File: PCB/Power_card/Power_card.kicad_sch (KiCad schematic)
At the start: 55 parts, among them J1 Conn_01x01_Pin, J2 Conn_01x01_Pin, J3 Conn_01x01_Pin, J4 Conn_01x01_Pin, J5 Conn_01x01_Pin, J6 Conn_01x01_Pin, J7 Conn_02x04_Counter_Clockwise, J8 Conn_01x01_Pin, K1 Relay_SPST-NO, K2 Relay_SPST-NO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

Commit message: Ajout crystal
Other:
- note added: "Power card for touch switch"
- note removed: "Touch switch prototype"

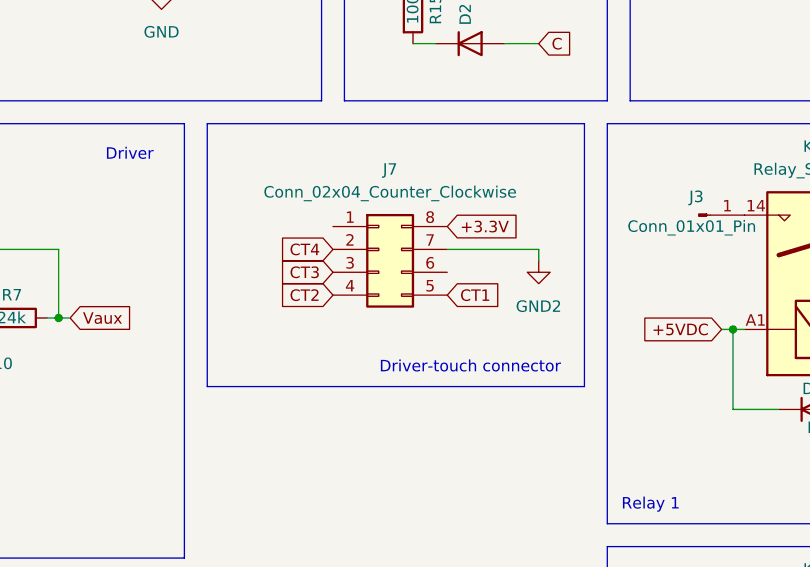
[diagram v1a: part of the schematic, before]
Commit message: Changement de connecteurs
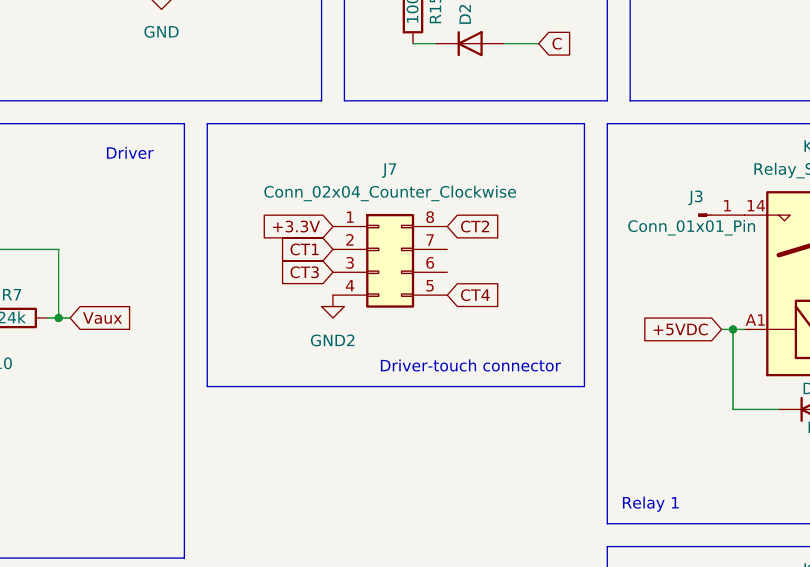
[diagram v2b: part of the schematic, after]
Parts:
- J7: footprint Connector_PinSocket_2.54mm:PinSocket_2x04_P2.54mm_Vertical -> Touch_Switch_Custom:Pin femelle
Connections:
- net +3.3V: now also J7.1 (Pin_1); no longer J7.8 (Pin_8)
- net CT1: now also J7.2 (Pin_2); no longer J7.5 (Pin_5)
- net CT2: now also J7.8 (Pin_8); no longer J7.4 (Pin_4)
- net CT4: now also J7.5 (Pin_5); no longer J7.2 (Pin_2)
- net GND2: now also J7.4 (Pin_4); no longer J7.7 (Pin_7)
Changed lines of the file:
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@@
 	(wire
 		(pts
-			(xy 137.16 83.82) (xy 147.32 83.82)
-		)
-		(stroke
-			(width 0)
-			(type default)
-		)
-	)
-	(wire
-		(pts
 			(xy 92.71 44.45) (xy 90.17 44.45)
 		)
@@
 	(wire
 		(pts
-			(xy 147.32 83.82) (xy 147.32 85.09)
-		)
-		(stroke
-			(width 0)
-			(type default)
-		)
-	)
-	(wire
-		(pts
 			(xy 105.41 41.91) (xy 105.41 45.72)
 		)
@@
 		)
 	)
+	(global_label "CT4"
+		(shape input)
+		(at 137.16 88.9 0)
+		(fields_autoplaced yes)
+		(effects
+			(font
+				(size 1.27 1.27)
+			)
+			(justify left)
+		)
+		(property "Intersheetrefs" "${INTERSHEET_REFS}"
+			(at 143.5923 88.9 0)
+			(effects
+				(font
+					(size 1.27 1.27)
+				)
+				(justify left)
+				(hide yes)
+			)
+		)
+	)
 	(global_label "VCC_IC"
 		(shape input)
@@
 		)
 	)
+	(global_label "CT2"
+		(shape input)
+		(at 137.16 81.28 0)
+		(fields_autoplaced yes)
+		(effects
+			(font
+				(size 1.27 1.27)
+			)
+			(justify left)
+		)
+		(property "Intersheetrefs" "${INTERSHEET_REFS}"
+			(at 143.5923 81.28 0)
+			(effects
+				(font
+					(size 1.27 1.27)
+				)
+				(justify left)
+				(hide yes)
+			)
+		)
+	)
 	(global_label "N"
 		(shape input)
@@
 		)
 	)
-	(global_label "CT2"
+	(global_label "CT3"
 		(shape input)
-		(at 124.46 88.9 180)
+		(at 124.46 86.36 180)
 		(fields_autoplaced yes)
 		(effects
@@
 		)
 		(property "Intersheetrefs" "${INTERSHEET_REFS}"
-			(at 118.0277 88.9 0)
+			(at 118.0277 86.36 0)
 			(effects
 				(font
@@
 		)
 	)
-	(global_label "+3.3V"
+	(global_label "CT1"
 		(shape input)
-		(at 137.16 81.28 0)
+		(at 200.66 96.52 90)
 		(fields_autoplaced yes)
 		(effects
@@
 		)
 		(property "Intersheetrefs" "${INTERSHEET_REFS}"
-			(at 145.83 81.28 0)
+			(at 200.66 90.0877 90)
 			(effects
 				(font
@@
 		)
 	)
-	(global_label "CT1"
+	(global_label "+3.3V"
 		(shape input)
-		(at 137.16 88.9 0)
+		(at 124.46 81.28 180)
 		(fields_autoplaced yes)
 		(effects
@@
 				(size 1.27 1.27)
 			)
-			(justify left)
+			(justify right)
 		)
 		(property "Intersheetrefs" "${INTERSHEET_REFS}"
-			(at 143.5923 88.9 0)
+			(at 115.79 81.28 0)
 			(effects
 				(font
 					(size 1.27 1.27)
 				)
-				(justify left)
+				(justify right)
 				(hide yes)
 			)
 		)
 	)
-	(global_label "CT1"
+	(global_label "L"
 		(shape input)
-		(at 200.66 96.52 90)
+		(at 240.03 82.55 0)
 		(fields_autoplaced yes)
 		(effects
@@
 		)
 		(property "Intersheetrefs" "${INTERSHEET_REFS}"
-			(at 200.66 90.0877 90)
+			(at 244.0433 82.55 0)
 			(effects
 				(font
@@
 		)
 	)
-	(global_label "CT4"
+	(global_label "CT1"
 		(shape input)
 		(at 124.46 83.82 180)
@@
 		)
 	)
-	(global_label "L"
-		(shape input)
-		(at 240.03 82.55 0)
-		(fields_autoplaced yes)
-		(effects
-			(font
-				(size 1.27 1.27)
-			)
-			(justify left)
-		)
-		(property "Intersheetrefs" "${INTERSHEET_REFS}"
-			(at 244.0433 82.55 0)
-			(effects
-				(font
-					(size 1.27 1.27)
-				)
-				(justify left)
-				(hide yes)
-			)
-		)
-	)
 	(global_label "+310VDC"
 		(shape input)
@@
 		)
 	)
-	(global_label "CT3"
-		(shape input)
-		(at 124.46 86.36 180)
-		(fields_autoplaced yes)
-		(effects
-			(font
-				(size 1.27 1.27)
-			)
-			(justify right)
-		)
-		(property "Intersheetrefs" "${INTERSHEET_REFS}"
-			(at 118.0277 86.36 0)
-			(effects
-				(font
-					(size 1.27 1.27)
-				)
-				(justify right)
-				(hide yes)
-			)
-		)
-	)
 	(global_label "+5VDC"
 		(shape input)
@@
 			)
 		)
-		(property "Footprint" "Connector_PinSocket_2.54mm:PinSocket_2x04_P2.54mm_Vertical"
+		(property "Footprint" "Touch_Switch_Custom:Pin femelle"
 			(at 129.54 83.82 0)
 			(effects
@@
 	)
 	(symbol
-		(lib_id "power:GND2")
-		(at 147.32 85.09 0)
-		(unit 1)
-		(exclude_from_sim no)
-		(in_bom yes)
-		(on_board yes)
-		(dnp no)
-		(fields_autoplaced yes)
-		(property "Reference" "#PWR010"
-			(at 147.32 91.44 0)
-			(effects
-				(font
-					(size 1.27 1.27)
-				)
-				(hide yes)
-			)
-		)
-		(property "Value" "GND2"
-			(at 147.32 90.17 0)
-			(effects
-				(font
-					(size 1.27 1.27)
-				)
-			)
-		)
-		(property "Footprint" ""
-			(at 147.32 85.09 0)
-			(effects
-				(font
-					(size 1.27 1.27)
-				)
-				(hide yes)
-			)
-		)
-		(property "Datasheet" ""
-			(at 147.32 85.09 0)
-			(effects
-				(font
-					(size 1.27 1.27)
-				)
-				(hide yes)
-			)
-		)
-		(property "Description" "Power symbol creates a global label with name \"GND2\" , ground"
-			(at 147.32 85.09 0)
-			(effects
-				(font
-					(size 1.27 1.27)
-				)
-				(hide yes)
-			)
-		)
-		(pin "1"
-		)
-		(instances
-			(project "Power_card"
-				(path "/6e223a1a-ee81-40df-b8c9-24ff3e142a46"
-					(reference "#PWR010")
-					(unit 1)
-				)
-			)
-		)
-	)
-	(symbol
 		(lib_id "Relay:Relay_SPST-NO")
 		(at 232.41 134.62 90)
@@
 					(unit 1)
 				)
+			)
+		)
+	)
+	(symbol
+		(lib_id "power:GND2")
+		(at 124.46 88.9 0)
+		(unit 1)
+		(exclude_from_sim no)
+		(in_bom yes)
+		(on_board yes)
+		(dnp no)
+		(fields_autoplaced yes)
+		(property "Reference" "#PWR02"
+			(at 124.46 95.25 0)
+			(effects
+				(font
+					(size 1.27 1.27)
+				)
+				(hide yes)
+			)
+		)
+		(property "Value" "GND2"
+			(at 124.46 93.98 0)
+			(effects
+				(font
+					(size 1.27 1.27)
+				)
+			)
+		)
+		(property "Footprint" ""
+			(at 124.46 88.9 0)
+			(effects
+				(font
+					(size 1.27 1.27)
+				)
+				(hide yes)
+			)
+		)
+		(property "Datasheet" ""
+			(at 124.46 88.9 0)
+			(effects
+				(font
+					(size 1.27 1.27)
+				)
+				(hide yes)
+			)
+		)
+		(property "Description" "Power symbol creates a global label with name \"GND2\" , ground"
+			(at 124.46 88.9 0)
+			(effects
+				(font
+					(size 1.27 1.27)
+				)
+				(hide yes)
+			)
+		)
+		(pin "1"
+		)
+		(instances
+			(project "Power_card"
+				(path "/6e223a1a-ee81-40df-b8c9-24ff3e142a46"
+					(reference "#PWR02")
+					(unit 1)
+				)

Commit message: Ajout des footprints
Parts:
- J7: footprint Touch_Switch_Custom:Pin femelle -> Touch_Switch_Custom:PinFemelle
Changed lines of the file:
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@@
 			)
 		)
-		(property "Footprint" "Touch_Switch_Custom:Pin femelle"
+		(property "Footprint" "Touch_Switch_Custom:PinFemelle"
 			(at 129.54 83.82 0)
 			(effects
@@
 			)
 		)
-		(property "Datasheet" "~"
+		(property "Datasheet" ""
 			(at 129.54 83.82 0)
 			(effects
